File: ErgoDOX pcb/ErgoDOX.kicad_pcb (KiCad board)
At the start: 2 copper layers, 182.8 x 158.9 mm, 94 parts, among them J1 USB, J10 USB VCC, J2 3.5mm, J3 JMP, J4 JMP, J5 BT_JMP, J6 EN_JMP, J7 PROG, J8 JTAG, J9 USB GND, SW0:10 SW0:3, SW0:11 SW0:2, SW0:12 SW0:1, SW0:7 SW0:6, SW0:8 SW0:5, SW0:9 SW0:4, SW1:10 SW1:3, SW1:11 SW1:2, SW1:12 SW1:1, SW1:13 SW1:0, SW1:9 SW1:4, SW2:10 SW2:3, SW2:11 SW2:2, SW2:12 SW2:1, SW2:13 SW2:0, SW2:7 SW2:6, SW2:8 SW2:5, SW2:9 SW2:4, SW3:10 SW3:3, SW3:11 SW3:2, SW3:12 SW3:1, SW3:13 SW3:0, SW3:8 SW3:5, SW3:9 SW3:4, SW4:10 SW4:3, SW4:11 SW4:2, SW4:12 SW4:1, SW4:13 SW4:0, SW4:7 SW4:6, SW4:8 SW4:5, SW4:9 SW4:4, SW5:10 SW5:3, SW5:11 SW5:2, SW5:12 SW5:1, SW5:13 SW5:0, SW5:7 SW5:6, SW5:8 SW5:5, SW5:9 SW5:4, U1 LM337_SOT223, U2 ESP32-S3 LH, U3 ESP32-S3 RH

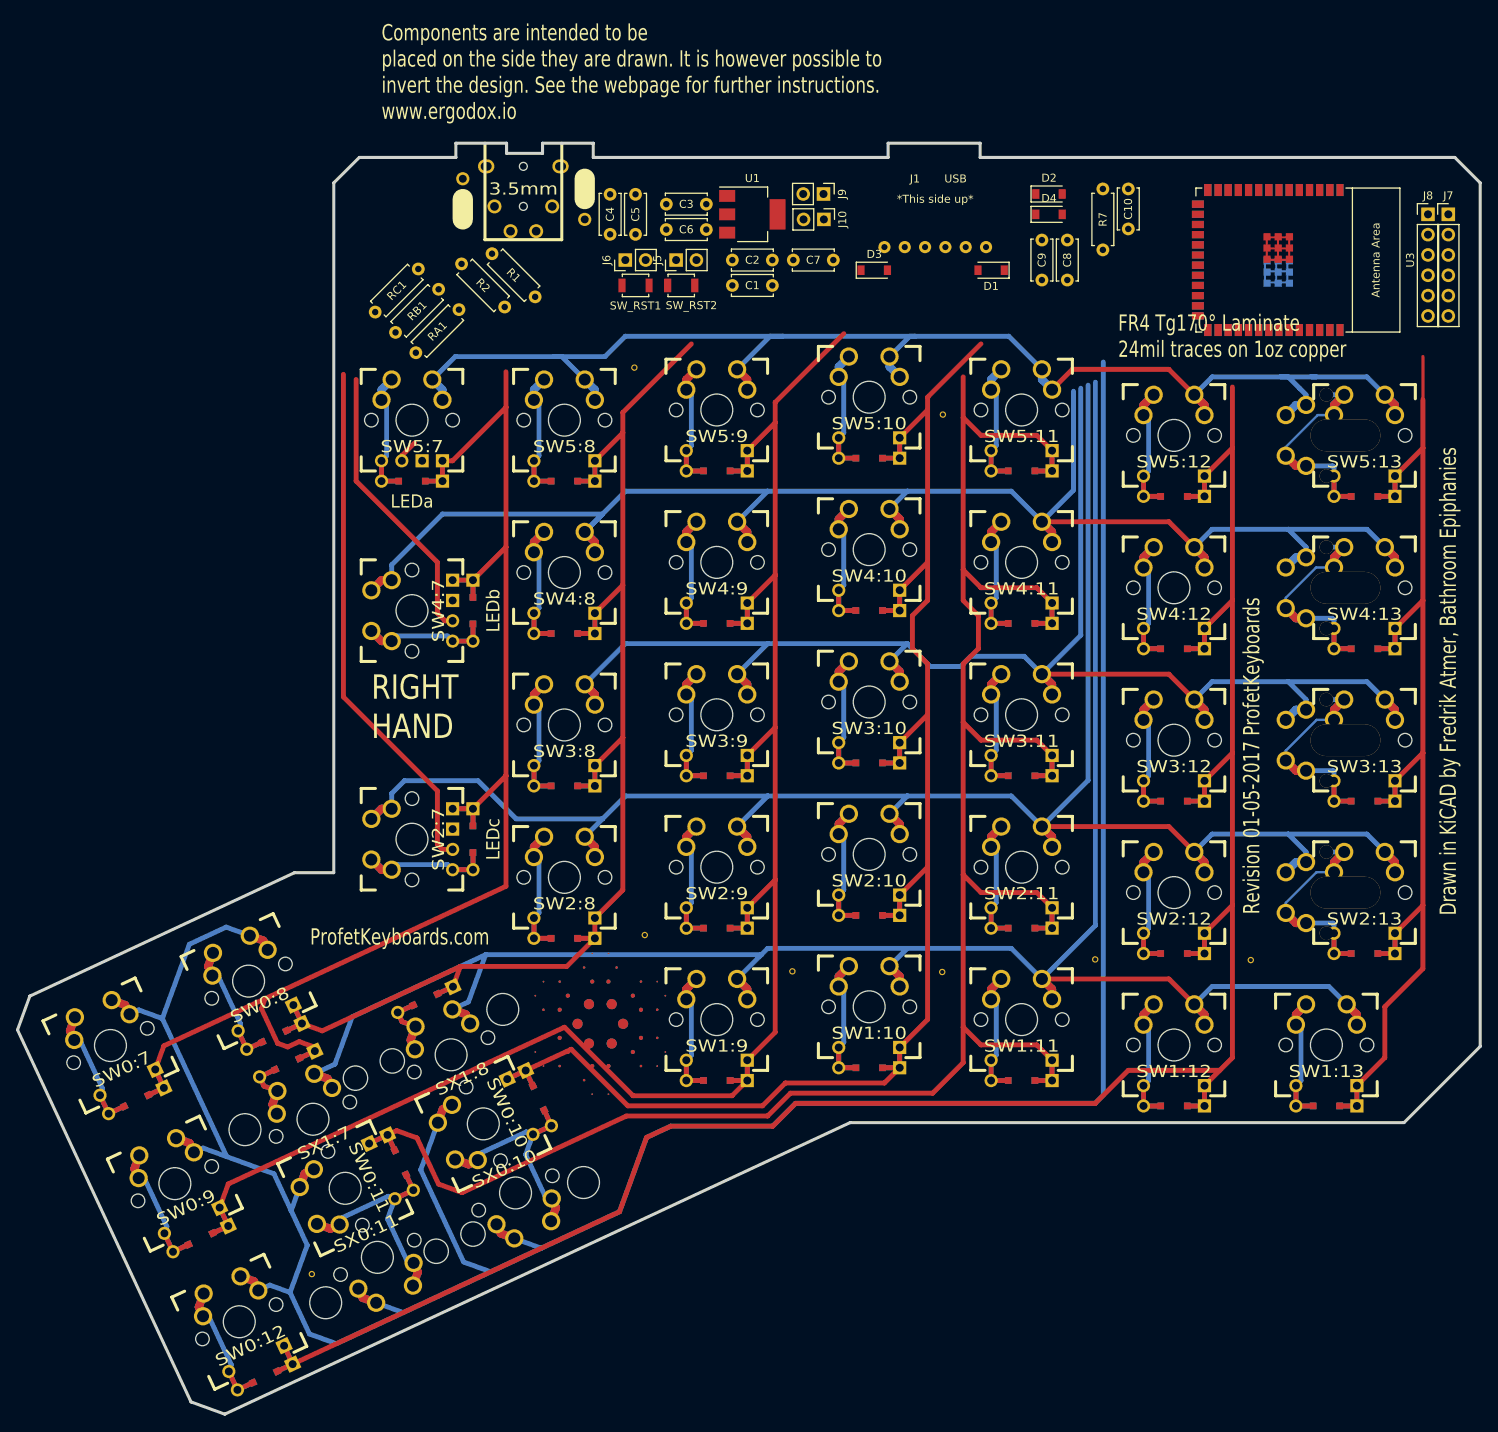
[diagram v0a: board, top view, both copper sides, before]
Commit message: First route of board
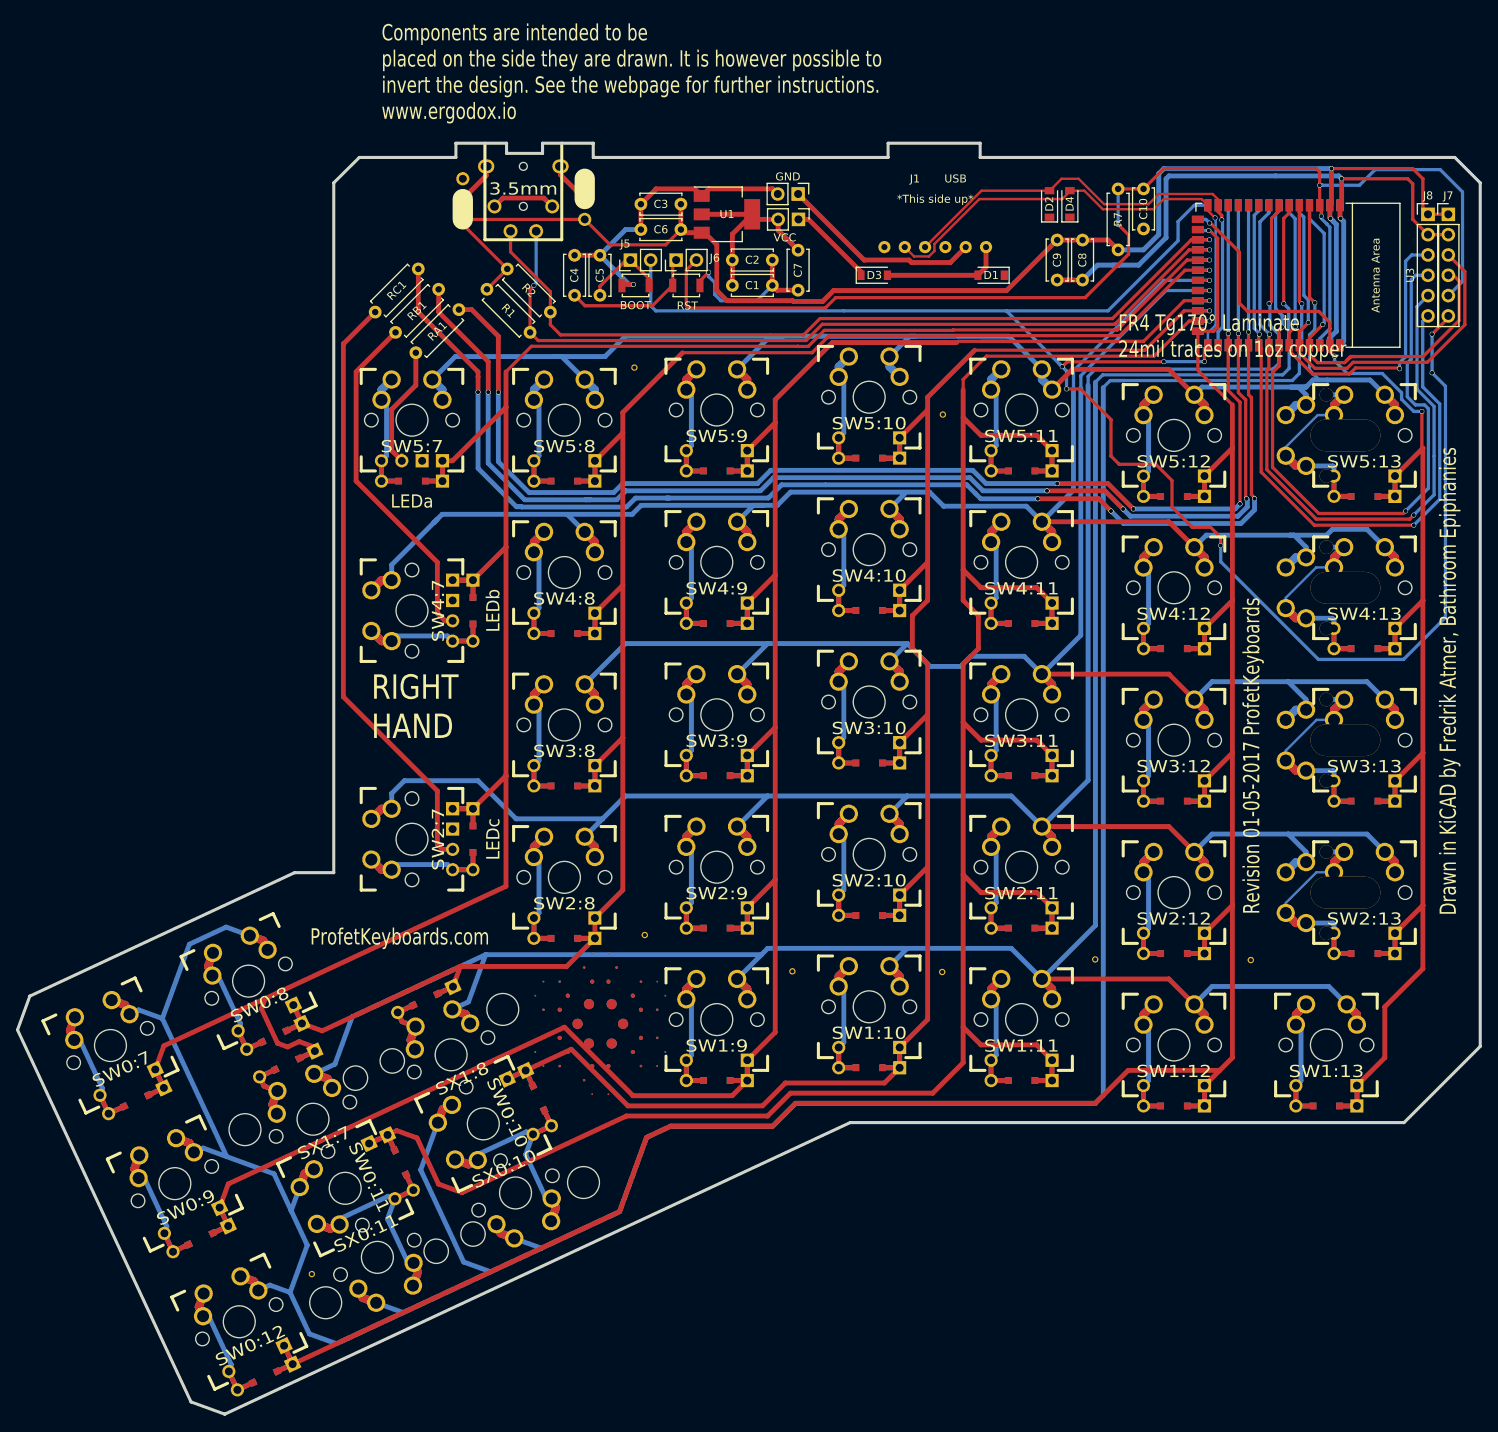
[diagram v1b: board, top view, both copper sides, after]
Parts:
- moved C4 8.82 mm to (92.7, 44.5)
- moved C5 8.82 mm to (95.9, 44.5)
- moved RST 6.35 mm to (106.7, 48.3)
- moved J6 6.35 mm to (105.4, 45.1)
- moved R2 5.75 mm to (84.3, 46.2)
- moved BOOT 5.72 mm to (100.3, 48.3)
- moved J5 5.72 mm to (99.7, 45.1)
- moved C7 4.57 mm to (120.7, 43.9), turned to -90 degrees
- moved R1 4.49 mm to (81.8, 48.7)
- moved C3 3.18 mm to (106.0, 38.1)
- moved C6 3.18 mm to (106.0, 41.3)
- moved GND 3.17 mm to (120.7, 36.8)
- moved U1 3.17 mm to (111.8, 39.4)
- moved VCC 3.17 mm to (120.7, 40.0)
- moved D4 2.91 mm to (154.6, 38.1), turned to 90 degrees
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- renumbered SW_RST2 to BOOT, J9 to GND, SW_RST1 to RST, J10 to VCC
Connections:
- J2 pad 3: /SCLM -> /esp_lh/SDAM
- J2 pad 5: /SCLM -> /esp_lh/SCLM
- J7 pad 3: U0TXD -> U0RXD
- J7 pad 4: U0RXD -> U0TXD
- SW0:11 pad 4: COL11 -> COL2
- SW1:11 pad 4: COL11 -> COL2
- SW2:11 pad 4: COL11 -> COL2
- SW3:11 pad 4: COL11 -> COL2
- SW4:11 pad 4: COL11 -> COL2
- SW5:11 pad 4: COL11 -> COL2
- U2 pad 16: COL6 -> COL2
- U2 pad 17: /esp_lh/SCLM -> COL3
- U2 pad 18: /esp_lh/SDAM -> COL4
- U2 pad 19: ROW1 -> ROW3
- U2 pad 20: ROW0 -> ROW4
- U2 pad 22: COL4 -> COL6
- U2 pad 23: COL3 -> /esp_lh/SDAM
- U2 pad 24: COL11 -> /esp_lh/SCLM
- U2 pad 29: LED_C -> LED_A
- U2 pad 31: LED_A -> LED_C
- U2 pad 5: ROW4 -> ROW0
- U2 pad 6: ROW3 -> ROW1
- U3 pad 16: COL0 -> unconnected-(U3-Pad16)
- U3 pad 19: ROW1 -> COL6
- U3 pad 20: ROW0 -> COL5
- U3 pad 21: COL1 -> ROW4
- U3 pad 22: COL11 -> ROW3
- U3 pad 23: COL3 -> COL4
- U3 pad 24: COL4 -> COL3
- U3 pad 25: COL5 -> COL2
- U3 pad 26: COL6 -> COL1
- U3 pad 29: LED_B -> LED_A
- U3 pad 30: LED_A -> LED_B
- U3 pad 31: unconnected-(U3-Pad31) -> LED_C
- U3 pad 39: unconnected-(U3-Pad39) -> COL0
- U3 pad 5: ROW4 -> ROW0
- U3 pad 6: ROW3 -> ROW1
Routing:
- net COL2: track 0.00 -> 297.8 mm, vias 0 -> 1
- net COL11: track 262.9 -> 0.00 mm
- net /BOOT: track 0.00 -> 225.7 mm, vias 0 -> 7
- net VCC: track 0.00 -> 187.4 mm, vias 0 -> 2
- net LED_C: track 0.00 -> 169.8 mm, vias 0 -> 5
- net LED_B: track 0.00 -> 163.8 mm, vias 0 -> 5
- net LED_A: track 0.00 -> 157.6 mm, vias 0 -> 5
- net /EN: track 0.00 -> 155.8 mm, vias 0 -> 3
- net GND: track 0.00 -> 145.3 mm, vias 0 -> 4
- net /esp_lh/SDAM: track 0.00 -> 104.7 mm, vias 0 -> 2
- net /esp_lh/SCLM: track 0.00 -> 103.2 mm, vias 0 -> 1
- net COL6: track 168.8 -> 264.2 mm, vias 0 -> 1
- net TDI: track 0.00 -> 87.3 mm, vias 0 -> 2
- net TDO: track 0.00 -> 85.2 mm, vias 0 -> 2
- net TCK: track 0.00 -> 84.5 mm, vias 0 -> 2
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
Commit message: Add back components, silk screen
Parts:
- removed BOOT: BOOT, Button_Switch_SMD:SW_SPST_B3U-1000P
- removed GND: USB GND, Connector_PinHeader_2.54mm:PinHeader_1x02_P2.54mm_Vertical
- removed RST: RST, Button_Switch_SMD:SW_SPST_B3U-1000P
- removed VCC: USB VCC, Connector_PinHeader_2.54mm:PinHeader_1x02_P2.54mm_Vertical
- added ?: , , F.Cu at (47.9, 146.9)
- added ?: , , F.Cu at (199.4, 140.6)
- added ?: , , F.Cu at (139.3, 91.2)
- added ?: , , F.Cu at (58.8, 117.2)
- added ?: , , F.Cu at (107.7, 158.5)
- added D5: SMF9.0CA, Diode_SMD:D_SOD-123, B.Cu at (143.4, 48.5)
- added D6: SMF9.0CA, Diode_SMD:D_SOD-123, B.Cu at (152.1, 38.1)
- added D7: SMF9.0CA, Diode_SMD:D_SOD-123, B.Cu at (154.7, 38.1)
- added D8: 1N5819HW-7-F, Diode_SMD:D_SOD-123, B.Cu at (128.8, 48.5)
- added J10: USB VCC, Connector_PinHeader_2.54mm:PinHeader_1x02_P2.54mm_Vertical, F.Cu at (120.7, 40.0)
- added J11: USB_LH, ErgoDOX pcb:SF USB-C Breakout, B.Cu at (137.8, 39.6)
- added J9: USB GND, Connector_PinHeader_2.54mm:PinHeader_1x02_P2.54mm_Vertical, F.Cu at (120.7, 37.0)
- added REF**: MountingHole_2.1mm, MountingHole:MountingHole_2.1mm, F.Cu at (44.7, 38.7)
- added SW_RST1: RST, Button_Switch_SMD:SW_SPST_B3U-1000P, F.Cu at (106.7, 48.4)
- added SW_RST2: BOOT, Button_Switch_SMD:SW_SPST_B3U-1000P, F.Cu at (100.2, 48.5)
- added SW_RST3: BOOT_LH, Button_Switch_SMD:SW_SPST_B3U-1000P, B.Cu at (100.2, 48.5)
- added SW_RST4: RST_LH, Button_Switch_SMD:SW_SPST_B3U-1000P, B.Cu at (106.7, 48.4)
- added U4: LM337_SOT223, Package_TO_SOT_SMD:SOT-223-3_TabPin2, B.Cu at (111.8, 39.4)
- J1: value USB -> USB_RH
- moved D3 2.07 mm to (128.8, 48.5)
- moved D1 2.07 mm to (143.4, 48.5)
- moved C4 2.05 mm to (93.0, 46.5)
- moved C5 2.03 mm to (95.9, 46.5)
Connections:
- net Net-(C4-Pad2) renamed /EN_JMP
- net Net-(C5-Pad2) renamed /BT_JUMP
- net Net-(D1-Pad2) renamed /VBUS
- D3 pad 1: Net-(D3-Pad1) -> /USB_VCC
- J1 pad 2: Net-(J1-Pad2) -> /GBUS
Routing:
- net /GBUS: track 0.00 -> 35.4 mm
- net Net-(J1-Pad2): track 25.3 -> 0.00 mm
- net /USB_VCC: track 0.00 -> 14.5 mm, vias 0 -> 3
- net D+: track 62.4 -> 74.8 mm, vias 1 -> 2
- net GND: track 145.3 -> 157.4 mm
- net /VBUS: track 15.3 -> 27.3 mm, vias 0 -> 6
- net Net-(D3-Pad1): track 11.0 -> 0.00 mm
- net VCC: track 187.4 -> 198.2 mm, vias 2 -> 5
- net VCC_5V: track 24.6 -> 34.4 mm
- net D-: track 61.0 -> 68.6 mm, vias 1 -> 2
- net /BT_JUMP: track 10.4 -> 14.6 mm, vias 0 -> 1
- net /EN_JMP: track 17.2 -> 20.1 mm, vias 0 -> 1
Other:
- board text added: "Design by Dominic Beauchamp, based on the Key64 by Nestor A. Diaz Revised by Josiah Smith"
- board text added: "Drawn in KiCAD by Fredrik Atmer, Bathroom Epiphanies Revised by Josiah Smith"
- board text added: "Revised 02-20-2023 ohea.xyz"
- board text added: "ohea.xyz"
- board text added: "oheaDox"
- board text removed: "Design by Dominic Beauchamp, based on the Key64 by Nestor A. Diaz"
- board text removed: "Drawn in KiCAD by Fredrik Atmer, Bathroom Epiphanies"
- board text removed: "ErgoDox"
- board text removed: "ProfetKeyboards.com"
- board text removed: "Revision 01-05-2017 ProfetKeyboards"

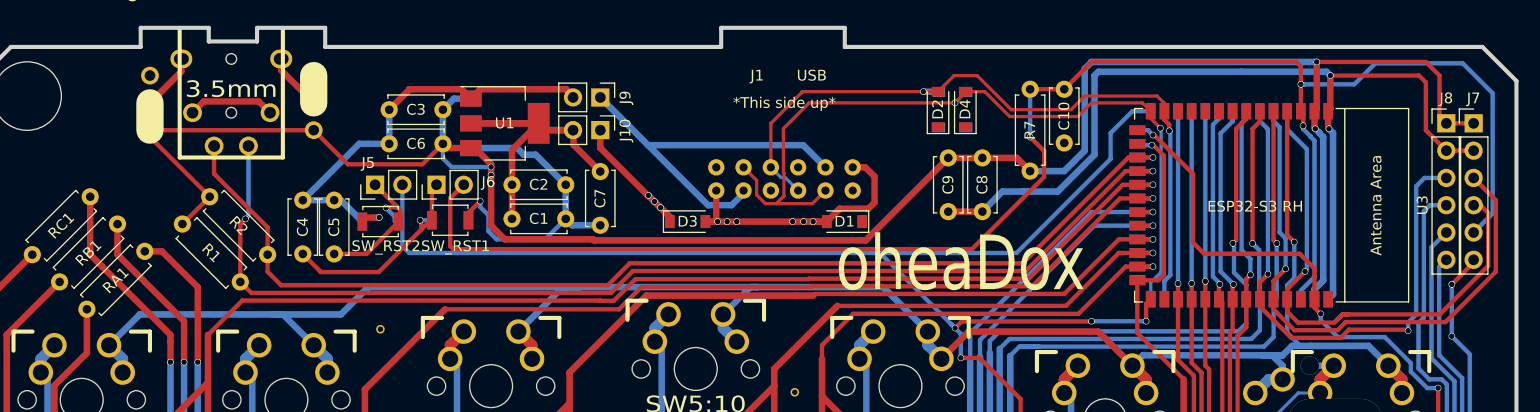
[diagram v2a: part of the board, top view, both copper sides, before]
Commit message: Add silkscreen notes and logo
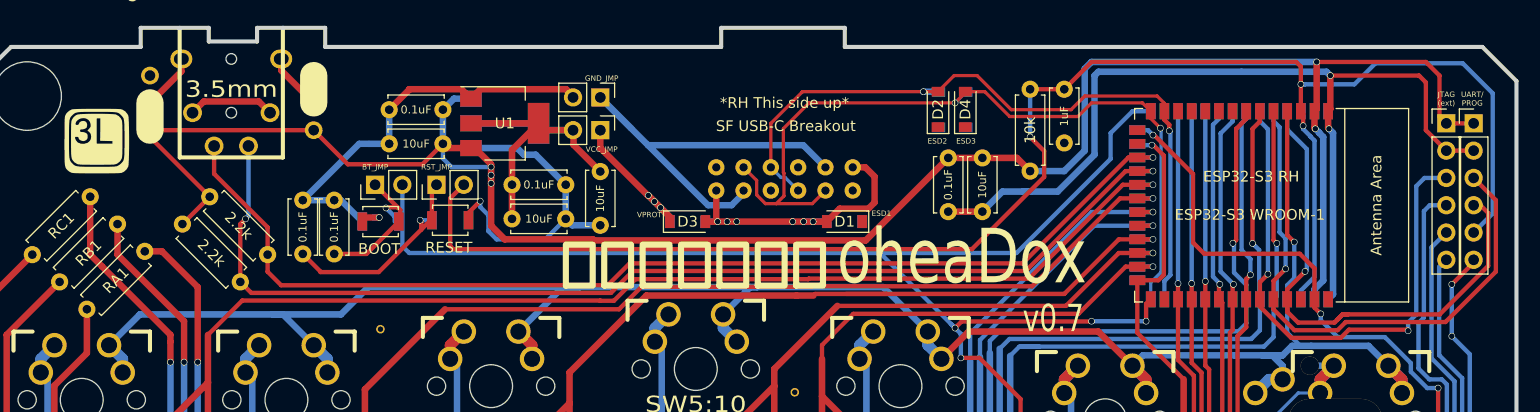
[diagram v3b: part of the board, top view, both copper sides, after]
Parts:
- added G***: LOGO, ErgoDOX pcb:3l_logo, F.Cu at (73.8, 41.0)
- added G***: LOGO, ErgoDOX pcb:3l_logo, B.Cu at (73.8, 41.0)
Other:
- board text added: "0.1uF"
- board text added: "10k"
- board text added: "10uF"
- board text added: "1uF"
- board text added: "2.2k"
- board text added: "BOOT"
- board text added: "BT_JMP"
- board text added: "ESD1"
- board text added: "ESD2"
- board text added: "ESD3"
- board text added: "ESP32-S3 WROOM-1"
- board text added: "GND_JMP"
- board text added: "JTAG (ext)"
- board text added: "RESET"
- board text added: "RST_JMP"
- board text added: "SF USB-C Breakout"
- board text added: "UART/ PROG"
- board text added: "VCC_JMP"
- board text added: "VPROT"
- board text added: "v0.7"
- board text added: "オヘアドックス"
